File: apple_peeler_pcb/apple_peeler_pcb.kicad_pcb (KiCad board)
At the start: 4 copper layers, 67 x 83 mm, 139 parts, among them J1 BM03B-SRSS-TB, J2 BM03B-SRSS-TB, J3 HYC10-HDMIA19-600B, J4 Header_01x06, J5 Header_01x06, J6 HYC10-HDMIA19-600B, J7 Header_01x02, J8 USB_C_Receptacle_USB2.0_16P, Q1 2N7002, Q10 2N7002, Q11 2N7002, Q12 2N7002, Q13 2N7002, Q14 AO3401A, Q15 2N7002, Q16 AO3401A, Q17 2N7002, Q18 2N7002, Q2 2N7002, Q3 2N7002, Q4 2N7002, Q5 2N7002, Q6 2N7002, Q7 2N7002, Q8 2N7002, Q9 2N7002, SW1 SPST BTN, SW2 SPST BTN, SW3 SPST BTN, U1 W25Q16JVSS, U2 RP2040, U3 4066, U4 TPS562242, Y1 12MHz

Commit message: fix clearance-related DRC and "fix" silkscreen-related DRC
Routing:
- net GND: track 65.9 -> 66.3 mm, vias 166 -> 167

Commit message: some final touches to HDMI layout
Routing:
- net GND: track 66.3 -> 58.9 mm
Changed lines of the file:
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@@
 	)
 	(segment
-		(start 212.2525 103.5)
-		(end 212.2525 103.5)
-		(width 0.3)
-		(layer "F.Cu")
-		(net 2)
-	)
-	(segment
 		(start 196.5325 116.8975)
 		(end 196.35375 116.71875)
@@
 	)
 	(segment
-		(start 212.2525 102)
-		(end 212.2525 102)
-		(width 0.3)
-		(layer "F.Cu")
-		(net 2)
-	)
-	(segment
 		(start 176.5275 128.2725)
 		(end 175.85 128.2725)
@@
 	)
 	(segment
-		(start 161.4 105.5)
-		(end 163.5 105.5)
-		(width 0.3)
-		(layer "F.Cu")
-		(net 2)
-	)
-	(segment
 		(start 160.57 151.105)
 		(end 161.9 151.105)
@@
 	)
 	(segment
-		(start 209.4975 105)
-		(end 212.2525 105)
-		(width 0.3)
-		(layer "F.Cu")
-		(net 2)
-	)
-	(segment
 		(start 194.55 149)
 		(end 193.5 149)
@@
 	)
 	(segment
-		(start 212.2525 102)
-		(end 209.4975 102)
-		(width 0.3)
-		(layer "F.Cu")
-		(net 2)
-	)
-	(segment
 		(start 200.66 119.04)
 		(end 200.9775 118.7225)
@@
 	)
 	(segment
-		(start 161.4 108.5)
-		(end 163.5 108.5)
-		(width 0.3)
-		(layer "F.Cu")
-		(net 2)
-	)
-	(segment
-		(start 209.4975 103.5)
-		(end 212.2525 103.5)
+		(start 209.4975 106.5)
+		(end 208 106.5)
 		(width 0.3)
 		(layer "F.Cu")
@@
 	)
 	(segment
-		(start 212.2525 106.5)
-		(end 212.2525 106.5)
-		(width 0.3)
-		(layer "F.Cu")
-		(net 2)
-	)
-	(segment
 		(start 188 134.05)
 		(end 188.2 134.05)
@@
 	)
 	(segment
+		(start 209.4975 103.5)
+		(end 208 103.5)
+		(width 0.3)
+		(layer "F.Cu")
+		(net 2)
+	)
+	(segment
+		(start 208 102)
+		(end 209.4975 102)
+		(width 0.3)
+		(layer "F.Cu")
+		(net 2)
+	)
+	(segment
 		(start 160.57 157.505)
 		(end 160.57 158.025)
@@
 	)
 	(segment
+		(start 165 110)
+		(end 163.5 110)
+		(width 0.3)
+		(layer "F.Cu")
+		(net 2)
+	)
+	(segment
 		(start 170.815 118.11)
 		(end 171.1325 118.4275)
@@
 	)
 	(segment
+		(start 165 107)
+		(end 163.5 107)
+		(width 0.3)
+		(layer "F.Cu")
+		(net 2)
+	)
+	(segment
 		(start 160.57 151.105)
 		(end 160.57 150.585)
@@
 	)
 	(segment
-		(start 161.4 107)
-		(end 163.5 107)
+		(start 165 108.5)
+		(end 163.5 108.5)
 		(width 0.3)
 		(layer "F.Cu")
@@
 	)
 	(segment
-		(start 161.4 110)
-		(end 163.5 110)
-		(width 0.3)
-		(layer "F.Cu")
-		(net 2)
-	)
-	(segment
 		(start 165.795 144.4025)
 		(end 165.4175 144.78)
@@
 	)
 	(segment
+		(start 165 105.5)
+		(end 163.5 105.5)
+		(width 0.3)
+		(layer "F.Cu")
+		(net 2)
+	)
+	(segment
 		(start 182.9975 121.5)
 		(end 182.2425 122.255)
@@
 	)
 	(segment
-		(start 155.8925 122.295)
-		(end 155.8925 121.285)
+		(start 209.4975 105)
+		(end 208 105)
 		(width 0.3)
 		(layer "F.Cu")
@@
 	)
 	(segment
-		(start 209.4975 106.5)
-		(end 212.2525 106.5)
+		(start 155.8925 122.295)
+		(end 155.8925 121.285)
 		(width 0.3)
 		(layer "F.Cu")
@@
 	)
 	(segment
-		(start 212.2525 105)
-		(end 212.2525 105)
-		(width 0.3)
-		(layer "F.Cu")
-		(net 2)
-	)
-	(segment
 		(start 160.9975 157.505)
 		(end 161.6075 158.115)
@@
 	)
 	(via
-		(at 161.4 108.5)
+		(at 165 108.5)
 		(size 0.5)
 		(drill 0.3)
@@
 	)
 	(via
-		(at 161.4 110)
+		(at 165 110)
 		(size 0.5)
 		(drill 0.3)
@@
 	)
 	(via
-		(at 212.2525 105)
+		(at 208 105)
 		(size 0.5)
 		(drill 0.3)
@@
 	)
 	(via
-		(at 161.4 105.5)
+		(at 165 105.5)
 		(size 0.5)
 		(drill 0.3)
@@
 	)
 	(via
-		(at 161.4 107)
+		(at 165 107)
 		(size 0.5)
 		(drill 0.3)
@@
 	)
 	(via
-		(at 212.2525 103.5)
+		(at 208 103.5)
 		(size 0.5)
 		(drill 0.3)
@@
 	)
 	(via
-		(at 172.900318 106.880804)
+		(at 172.429421 106.985332)
 		(size 0.5)
 		(drill 0.3)
@@
 	)
 	(via
-		(at 212.2525 106.5)
+		(at 208 106.5)
 		(size 0.5)
 		(drill 0.3)
@@
 	)
 	(via
-		(at 212.2525 102)
+		(at 208 102)
 		(size 0.5)
 		(drill 0.3)
@@
 	)
 	(segment
+		(start 172.514634 106.250366)
+		(end 179.041878 106.250366)
+		(width 0.127)
+		(layer "F.Cu")
+		(net 28)
+	)
+	(segment
+		(start 172.511916 106.253084)
+		(end 172.514634 106.250366)
+		(width 0.127)
+		(layer "F.Cu")
+		(net 28)
+	)
+	(segment
 		(start 188.618934 107.16255)
 		(end 188.618934 107.315)
@@
 	)
 	(segment
-		(start 179.041878 106.250366)
-		(end 180.436712 107.6452)
+		(start 171.767752 106.517752)
+		(end 171.767752 106.447173)
 		(width 0.127)
 		(layer "F.Cu")
@@
 	)
 	(segment
+		(start 180.436712 107.6452)
+		(end 187.446484 107.6452)
+		(width 0.127)
+		(layer "F.Cu")
+		(net 28)
+	)
+	(segment
 		(start 207.274693 106.609694)
 		(end 207.664999 107)
@@
 	)
 	(segment
-		(start 165.335001 105)
-		(end 165.669901 105.3349)
+		(start 171.767752 106.447173)
+		(end 171.961841 106.253084)
 		(width 0.127)
 		(layer "F.Cu")
@@
 	)
 	(segment
-		(start 188.618934 107.315)
-		(end 188.618934 107.63255)
+		(start 165.335001 105)
+		(end 165.669901 105.3349)
 		(width 0.127)
 		(layer "F.Cu")
@@
 	)
 	(segment
-		(start 172.085 106.68)
-		(end 172.514634 106.250366)
+		(start 188.618934 107.315)
+		(end 188.618934 107.63255)
 		(width 0.127)
 		(layer "F.Cu")
@@
 	)
 	(segment
-		(start 172.514634 106.250366)
-		(end 179.041878 106.250366)
+		(start 166.8185 105.3349)
+		(end 167.005 105.1484)
 		(width 0.127)
 		(layer "F.Cu")
@@
 	)
 	(segment
-		(start 180.436712 107.6452)
-		(end 187.446484 107.6452)
+		(start 171.961841 106.253084)
+		(end 172.511916 106.253084)
 		(width 0.127)
 		(layer "F.Cu")
@@
 	)
 	(segment
-		(start 166.8185 105.3349)
-		(end 167.005 105.1484)
+		(start 179.041878 106.250366)
+		(end 180.436712 107.6452)
 		(width 0.127)
 		(layer "F.Cu")
@@
 	)
 	(via
-		(at 172.085 106.68)
+		(at 171.767752 106.517752)
 		(size 0.5)
 		(drill 0.3)
@@
 	)
 	(segment
-		(start 171.3349 105.3349)
-		(end 167.1915 105.3349)
+		(start 171.767752 106.517752)
+		(end 171.767752 106.362752)
 		(width 0.127)
 		(layer "B.Cu")
@@
 	)
 	(segment
-		(start 172.085 106.68)
-		(end 171.752368 106.347368)
+		(start 167.1915 105.3349)
+		(end 167.005 105.1484)
 		(width 0.127)
 		(layer "B.Cu")
@@
 	)
 	(segment
-		(start 171.752368 106.347368)
-		(end 171.752368 105.752368)
+		(start 171.3349 105.3349)
+		(end 167.1915 105.3349)
 		(width 0.127)
 		(layer "B.Cu")
@@
 	)
 	(segment
-		(start 167.1915 105.3349)
-		(end 167.005 105.1484)
+		(start 171.767752 106.362752)
+		(end 171.752368 106.347368)
+		(width 0.127)
+		(layer "B.Cu")
+		(net 28)
+	)
+	(segment
+		(start 171.752368 106.347368)
+		(end 171.752368 105.752368)
 		(width 0.127)
 		(layer "B.Cu")

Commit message: change HDMI connector to one that's in stock
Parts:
- J3, J6: value HYC10-HDMIA19-600B -> HDMI-001 19PCBTP
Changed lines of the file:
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@@
 			)
 		)
-		(property "Value" "HYC10-HDMIA19-600B"
+		(property "Value" "HDMI-001 19PCBTP"
 			(at 1.715 10 0)
 			(layer "F.Fab")
@@
 			)
 		)
-		(property "LCSC" "C341098"
+		(property "LCSC" "C138388"
 			(at 0 0 0)
 			(unlocked yes)
@@
 		(sheetname "/Power supply/")
 		(sheetfile "power_supply.kicad_sch")
-		(attr through_hole)
+		(attr through_hole dnp)
 		(fp_line
 			(start -1.33 -1.33)
@@
 			)
 		)
-		(property "Value" "HYC10-HDMIA19-600B"
+		(property "Value" "HDMI-001 19PCBTP"
 			(at 1.715 10 0)
 			(layer "F.Fab")
@@
 			)
 		)
-		(property "LCSC" "C341098"
+		(property "LCSC" "C138388"
 			(at 0 0 180)
 			(unlocked yes)

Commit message: add JLC order number label
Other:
- board text added: "JLCJLCJLCJLC"
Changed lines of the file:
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@@
+		)
+	)
+	(gr_text "JLCJLCJLCJLC"
+		(at 186 92 0)
+		(layer "B.SilkS")
+		(effects
+			(font
+				(size 0.9 0.9)
+				(thickness 0.15)
+				(bold yes)
+			)
 		)
 	)

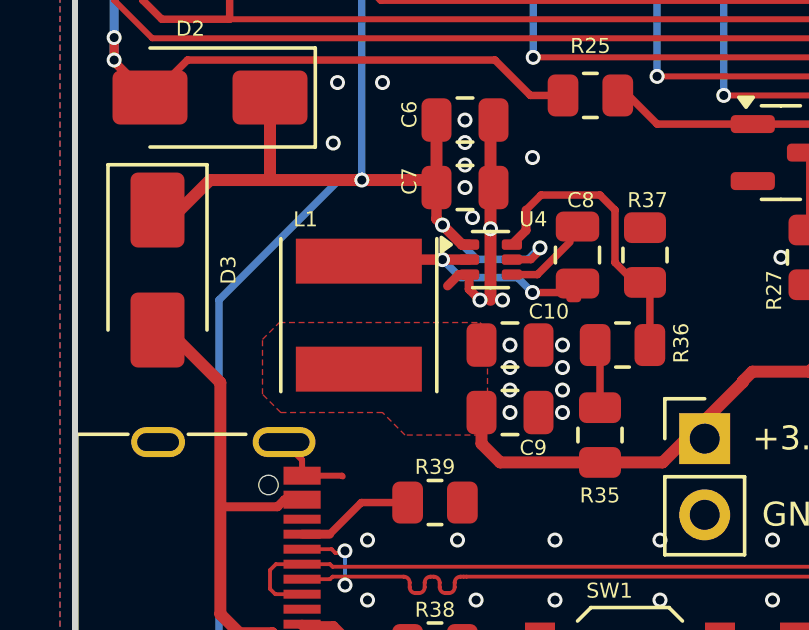
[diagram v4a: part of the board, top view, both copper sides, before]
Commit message: update SMPS inductor and divider
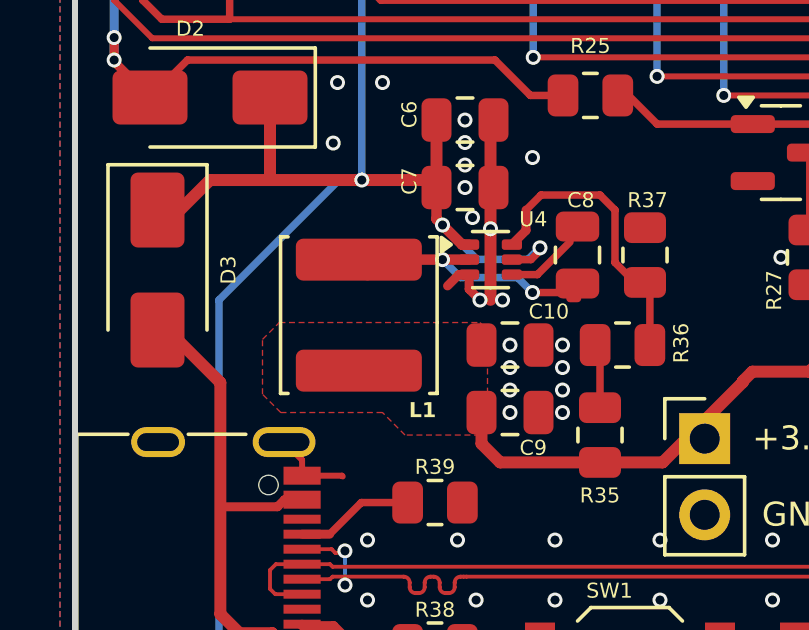
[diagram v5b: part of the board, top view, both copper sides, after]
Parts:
- L1: footprint Inductor_SMD:L_Taiyo-Yuden_MD-5050 -> Inductor_SMD:L_Sunlord_SWPA5020S
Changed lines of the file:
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@@
 		)
 	)
-	(footprint "Inductor_SMD:L_Taiyo-Yuden_MD-5050"
+	(footprint "Inductor_SMD:L_Sunlord_SWPA5020S"
 		(layer "F.Cu")
 		(at 162.461264 145.753573 -90)
-		(descr "Inductor, Taiyo Yuden, MD series, Taiyo-Yuden_MD-5050, 5.0mmx5.0mm")
-		(tags "inductor taiyo-yuden md smd")
+		(descr "Inductor, Sunlord, SWPA5020S, 5.0x5.0x2.0mm, (https://www.sunlordinc.com/UploadFiles/PDF_Cat/20120704094224784.pdf), generated with kicad-footprint-generator gen_inductor.py")
+		(tags "swpa")
 		(property "Reference" "L1"
-			(at -3.1925 1.7775 180)
+			(at 3.167758 -2.122951 0)
 			(layer "F.SilkS")
 			(effects
@@
 					(size 0.5 0.5)
 					(thickness 0.1)
+					(bold yes)
 				)
 			)
 		)
 		(property "Value" "1.5μH"
-			(at 0 4 90)
+			(at 0 3.45 270)
 			(layer "F.Fab")
 			(effects
 				(font
-					(size 0.5 0.5)
-					(thickness 0.1)
+					(size 1 1)
+					(thickness 0.15)
 				)
 			)
@@
 		(property "Datasheet" "~"
 			(at 0 0 270)
-			(unlocked yes)
 			(layer "F.Fab")
 			(hide yes)
@@
 				(font
 					(size 1.27 1.27)
-					(thickness 0.1)
+					(thickness 0.15)
 				)
 			)
@@
 		(property "Description" "Inductor, small symbol"
 			(at 0 0 270)
-			(unlocked yes)
 			(layer "F.Fab")
 			(hide yes)
@@
 				(font
 					(size 1.27 1.27)
-					(thickness 0.1)
+					(thickness 0.15)
 				)
 			)
 		)
-		(property "LCSC" "C702825"
+		(property "LCSC" "C56803"
 			(at 0 0 270)
 			(unlocked yes)
@@
 			(effects
 				(font
-					(size 0.5 0.5)
-					(thickness 0.1)
+					(size 1 1)
+					(thickness 0.15)
 				)
 			)
 		)
-		(property "MPN" "BWVF005050201R5T00"
+		(property "MPN" "SWPA5020S1R5MT"
 			(at 0 0 270)
 			(unlocked yes)
@@
 			(effects
 				(font
-					(size 0.5 0.5)
-					(thickness 0.1)
+					(size 1 1)
+					(thickness 0.15)
 				)
 			)
@@
 		(attr smd)
 		(fp_line
-			(start -2.55 2.6)
-			(end 2.55 2.6)
+			(start -2.61 2.61)
+			(end -2.61 2.36)
+			(stroke
+				(width 0.12)
+				(type solid)
+			)
+			(layer "F.SilkS")
+		)
+		(fp_line
+			(start 2.61 2.61)
+			(end -2.61 2.61)
 			(stroke
 				(width 0.12)
@@
 		)
 		(fp_line
-			(start -2.55 -2.6)
-			(end 2.55 -2.6)
+			(start 2.61 2.36)
+			(end 2.61 2.61)
 			(stroke
 				(width 0.12)
@@
 		)
 		(fp_line
-			(start -2.8 2.75)
-			(end 2.8 2.75)
+			(start -2.61 -2.36)
+			(end -2.61 -2.61)
+			(stroke
+				(width 0.12)
+				(type solid)
+			)
+			(layer "F.SilkS")
+		)
+		(fp_line
+			(start -2.61 -2.61)
+			(end 2.61 -2.61)
+			(stroke
+				(width 0.12)
+				(type solid)
+			)
+			(layer "F.SilkS")
+		)
+		(fp_line
+			(start 2.61 -2.61)
+			(end 2.61 -2.36)
+			(stroke
+				(width 0.12)
+				(type solid)
+			)
+			(layer "F.SilkS")
+		)
+		(fp_line
+			(start -2.75 2.75)
+			(end -2.75 2.35)
 			(stroke
 				(width 0.05)
@@
 		)
 		(fp_line
-			(start 2.8 2.75)
-			(end 2.8 -2.75)
+			(start 2.75 2.75)
+			(end -2.75 2.75)
 			(stroke
 				(width 0.05)
@@
 		)
 		(fp_line
-			(start -2.8 -2.75)
-			(end -2.8 2.75)
+			(start -2.8 2.35)
+			(end -2.8 -2.35)
 			(stroke
 				(width 0.05)
@@
 		)
 		(fp_line
-			(start 2.8 -2.75)
-			(end -2.8 -2.75)
+			(start -2.75 2.35)
+			(end -2.8 2.35)
 			(stroke
 				(width 0.05)
@@
 		)
 		(fp_line
-			(start -2.5 2.5)
-			(end 2.5 2.5)
+			(start 2.75 2.35)
+			(end 2.75 2.75)
 			(stroke
-				(width 0.1)
+				(width 0.05)
 				(type solid)
 			)
-			(layer "F.Fab")
+			(layer "F.CrtYd")
 		)
 		(fp_line
-			(start 2.5 2.5)
-			(end 2.5 -2.5)
+			(start 2.8 2.35)
+			(end 2.75 2.35)
 			(stroke
-				(width 0.1)
+				(width 0.05)
 				(type solid)
 			)
-			(layer "F.Fab")
+			(layer "F.CrtYd")
 		)
 		(fp_line
-			(start -2.5 -2.5)
-			(end -2.5 2.5)
+			(start -2.8 -2.35)
+			(end -2.75 -2.35)
 			(stroke
-				(width 0.1)
+				(width 0.05)
 				(type solid)
 			)
-			(layer "F.Fab")
+			(layer "F.CrtYd")
+		)
+		(fp_line
+			(start -2.75 -2.35)
+			(end -2.75 -2.75)
+			(stroke
+				(width 0.05)
+				(type solid)
+			)
+			(layer "F.CrtYd")
+		)
+		(fp_line
+			(start 2.75 -2.35)
+			(end 2.8 -2.35)
+			(stroke
+				(width 0.05)
+				(type solid)
+			)
+			(layer "F.CrtYd")
+		)
+		(fp_line
+			(start 2.8 -2.35)
+			(end 2.8 2.35)
+			(stroke
+				(width 0.05)
+				(type solid)
+			)
+			(layer "F.CrtYd")
 		)
 		(fp_line
-			(start 2.5 -2.5)
-			(end -2.5 -2.5)
+			(start -2.75 -2.75)
+			(end 2.75 -2.75)
+			(stroke
+				(width 0.05)
+				(type solid)
+			)
+			(layer "F.CrtYd")
+		)
+		(fp_line
+			(start 2.75 -2.75)
+			(end 2.75 -2.35)
+			(stroke
+				(width 0.05)
+				(type solid)
+			)
+			(layer "F.CrtYd")
+		)
+		(fp_rect
+			(start -2.5 -2.5)
+			(end 2.5 2.5)
 			(stroke
 				(width 0.1)
 				(type solid)
 			)
+			(fill no)
 			(layer "F.Fab")
 		)
 		(fp_text user "${REFERENCE}"
-			(at 0 0 90)
+			(at 0 0 270)
 			(layer "F.Fab")
 			(effects
 				(font
-					(size 0.5 0.5)
-					(thickness 0.1)
+					(size 1 1)
+					(thickness 0.15)
 				)
 			)
 		)
-		(pad "1" smd rect
-			(at -1.8 0 270)
-			(size 1.5 4.2)
+		(pad "1" smd roundrect
+			(at -1.85 0 270)
+			(size 1.4 4.2)
 			(layers "F.Cu" "F.Mask" "F.Paste")
+			(roundrect_rratio 0.178571)
 			(net 8 "Net-(U4-SW)")
 			(pintype "passive")
 		)
-		(pad "2" smd rect
-			(at 1.8 0 270)
-			(size 1.5 4.2)
+		(pad "2" smd roundrect
+			(at 1.85 0 270)
+			(size 1.4 4.2)
 			(layers "F.Cu" "F.Mask" "F.Paste")
+			(roundrect_rratio 0.178571)
 			(net 10 "+3.3V")
 			(pintype "passive")
 		)
 		(embedded_fonts no)
-		(model "${KICAD9_3DMODEL_DIR}/Inductor_SMD.3dshapes/L_Taiyo-Yuden_MD-5050.step"
+		(model "${KICAD9_3DMODEL_DIR}/Inductor_SMD.3dshapes/L_Sunlord_SWPA5020S.step"
 			(offset
 				(xyz 0 0 0)
@@
 				(bold yes)
 			)
+			(justify mirror)
 		)
 	)

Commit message: correct inductor for smps
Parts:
- L1: value 1.5μH -> 2.2μH
- R35: value 6.2kΩ -> 1.5kΩ
- R36: value 39kΩ -> 30kΩ
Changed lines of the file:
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@@
 			)
 		)
-		(property "Value" "1.5μH"
+		(property "Value" "2.2μH"
 			(at 0 3.45 270)
 			(layer "F.Fab")
@@
 			)
 		)
-		(property "LCSC" "C56803"
+		(property "LCSC" "C279946"
 			(at 0 0 270)
 			(unlocked yes)
@@
 			)
 		)
-		(property "MPN" "SWPA5020S1R5MT"
+		(property "MPN" "SWPA5020S2R2MT"
 			(at 0 0 270)
 			(unlocked yes)
@@
 			)
 		)
-		(property "Value" "39kΩ"
+		(property "Value" "30kΩ"
 			(at 0 1.65 0)
 			(layer "F.Fab")
@@
 			)
 		)
-		(property "LCSC" "C25826"
+		(property "LCSC" "C17621"
 			(at 0 0 0)
 			(unlocked yes)
@@
 			)
 		)
-		(property "MPN" "R 39kΩ 125mW 0805"
+		(property "MPN" "R 30kΩ 125mW 0805"
 			(at 0 0 0)
 			(unlocked yes)
@@
 			)
 		)
-		(property "Value" "6.2kΩ"
+		(property "Value" "1.5kΩ"
 			(at 0 1.65 90)
 			(layer "F.Fab")
@@
 			)
 		)
-		(property "LCSC" "C17767"
+		(property "LCSC" "C4310"
 			(at 0 0 90)
 			(unlocked yes)
@@
 			)
 		)
-		(property "MPN" "R 6.2kΩ 125mW 0805"
+		(property "MPN" "R 1.5kΩ 125mW 0805"
 			(at 0 0 90)
 			(unlocked yes)

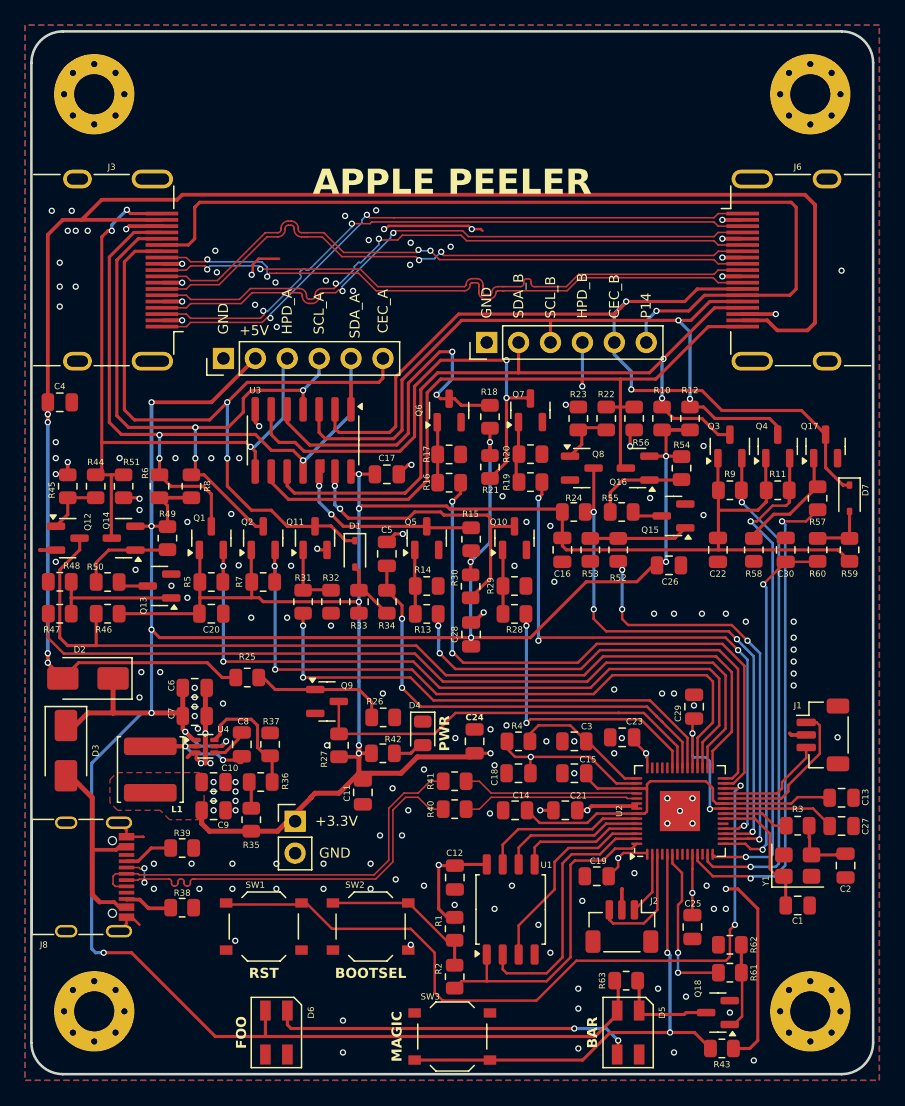
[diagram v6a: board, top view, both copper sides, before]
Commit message: replace fancy debug connectors by pin header to save $8
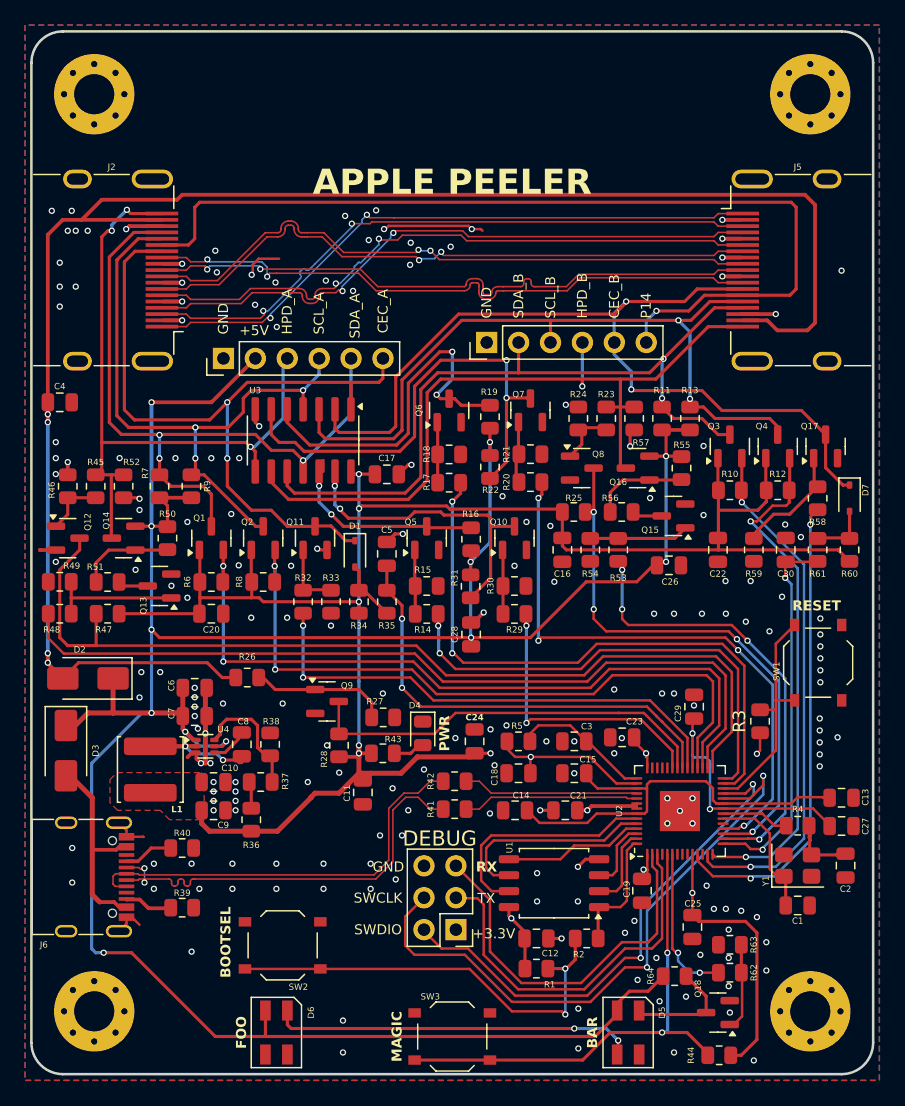
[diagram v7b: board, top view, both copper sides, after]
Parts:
- removed the J2 at (200.0, 158.2)
- removed J7: Header_01x02, conn:PinHeader_1x02_P2.54mm_Vertical
- added R3: 10kΩ, Resistor_SMD:R_0805_2012Metric, F.Cu at (211.0, 141.9)
- J1: value BM03B-SRSS-TB -> Header_2x03; footprint Connector_JST:JST_SH_BM03B-SRSS-TB_1x03-1MP_P1.00mm_Vertical -> conn:PinHeader_2x03_P2.54mm_Vertical
- moved SW1 48.9 mm to (215.6, 137.2), turned to -90 degrees
- moved J1 33.1 mm to (186.8, 158.5), turned to 180 degrees
- moved R2 10.9 mm to (197.2, 159.2), turned to 0 degrees
- moved C12 8.10 mm to (193.2, 159.2), turned to 0 degrees
- moved R1 7.24 mm to (193.2, 161.6), turned to 0 degrees
- moved SW2 7.16 mm to (173.0, 159.8), turned to 0 degrees
- moved U1 4.03 mm to (194.6, 154.8), turned to 180 degrees
- moved R64 3.87 mm to (204.2, 162.2)
- moved C19 3.78 mm to (201.6, 155.4), turned to -90 degrees
- moved R44 0.58 mm to (207.8, 168.5)
- renumbered J3 to J2, J4 to J3, J5 to J4, J6 to J5, J8 to J6, R9 to R10, R10 to R11, R11 to R12, R12 to R13, R13 to R14, R14 to R15, R15 to R16, R16 to R17, R17 to R18, R18 to R19, R19 to R20, R20 to R21, R21 to R22, R22 to R23, R23 to R24, R24 to R25, R25 to R26, R26 to R27, R27 to R28, R28 to R29, R29 to R30, R30 to R31, R31 to R32, R32 to R33, R33 to R34, R34 to R35, R35 to R36, R36 to R37, R37 to R38, R38 to R39, R3 to R4, R39 to R40, R40 to R41, R41 to R42, R42 to R43, R43 to R44, R44 to R45, R45 to R46, R46 to R47, R47 to R48, R48 to R49, R4 to R5, R49 to R50, R50 to R51, R51 to R52, R52 to R53, R53 to R54, R54 to R55, R55 to R56, R56 to R57, R57 to R58, R58 to R59, R5 to R6, R59 to R60, R60 to R61, R61 to R62, R62 to R63, R63 to R64, R6 to R7, R7 to R8, R8 to R9
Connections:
- J1 pad 1: Net-(J1-Pin_1) -> +3.3V
- J1 pad 2: GND -> Net-(J1-Pin_2)
- U2 pad 2: Net-(J2-Pin_1) -> Net-(J1-Pin_5)
- U2 pad 24: Net-(J1-Pin_1) -> Net-(J1-Pin_4)
- U2 pad 25: Net-(J1-Pin_3) -> Net-(J1-Pin_2)
- U2 pad 3: Net-(J2-Pin_3) -> Net-(J1-Pin_3)
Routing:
- net Net-(J1-Pin_4): track 0.00 -> 50.1 mm, vias 0 -> 2
- net Net-(U2-RUN): track 62.1 -> 18.8 mm, vias 2 -> 0
- net Net-(J1-Pin_2): track 0.00 -> 41.1 mm, vias 0 -> 2
- net Net-(J1-Pin_5): track 0.00 -> 30.4 mm
- net Net-(R1-Pad2): track 13.4 -> 34.8 mm, vias 0 -> 2
- net Net-(J1-Pin_3): track 8.91 -> 30.3 mm
- net /FLASH_CS: track 25.7 -> 9.96 mm
- net /FLASH_D1: track 20.8 -> 6.50 mm
- net Net-(J1-Pin_1): track 12.9 -> 0.00 mm
- net /FLASH_D2: track 16.0 -> 5.54 mm
- net Net-(J2-Pin_3): track 9.60 -> 0.00 mm
- net /FLASH_D3: track 13.1 -> 18.6 mm
- net Net-(J2-Pin_1): track 5.02 -> 0.00 mm
- net /FLASH_CLK: track 11.5 -> 16.4 mm
- net +3.3V: track 220.6 -> 224.6 mm
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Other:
- board text added: "RESET"
- board text removed: "RST"
